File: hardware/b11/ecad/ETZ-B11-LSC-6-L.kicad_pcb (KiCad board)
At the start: 2 copper layers, 112.3 x 85.8 mm, 0 parts

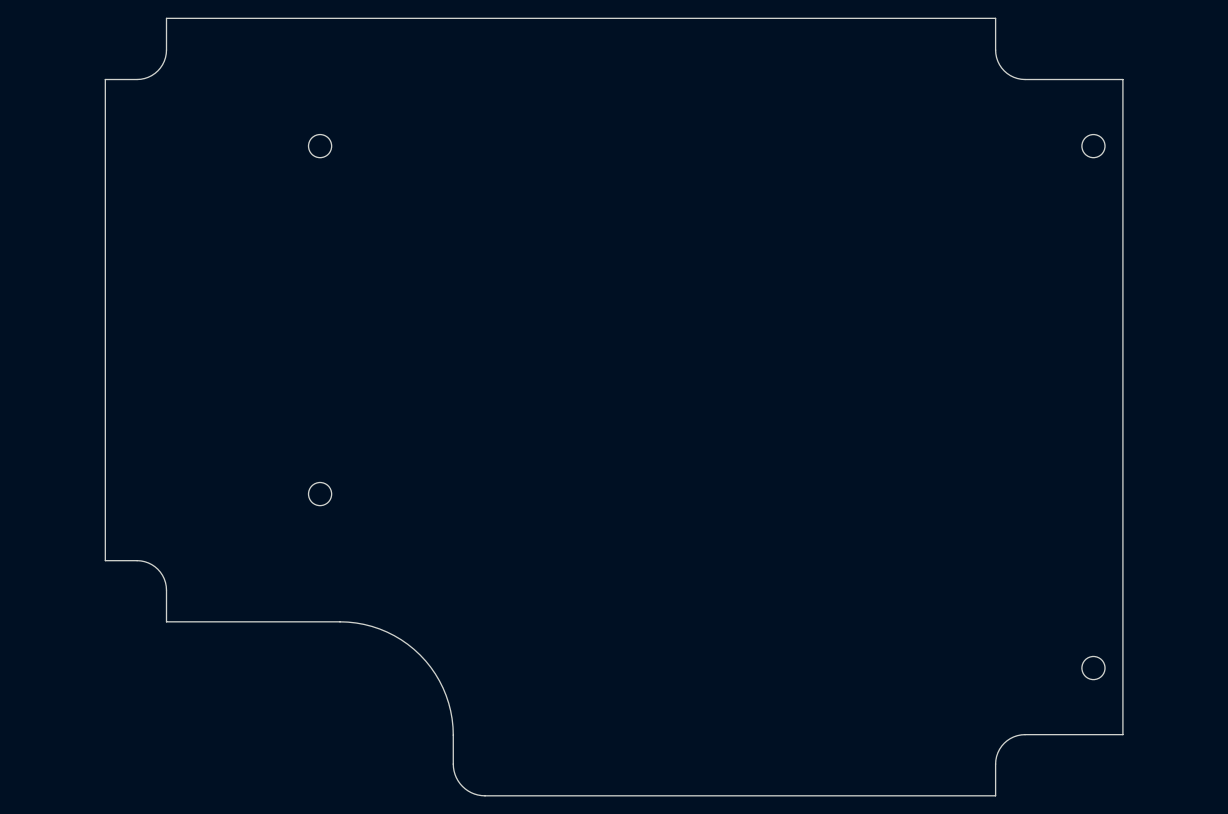
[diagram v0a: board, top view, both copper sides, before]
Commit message: fix(hardware/b11): correct 6-col PCB outlines and regenerate all boards
Update DXF outlines for all 6-col variants (LSC, RSC, LSP, RSP — both
normal and low profile) exported manually from OnShape with the _6
configuration. Regenerate all 16 KiCad PCBs from the corrected outlines
and re-place MX hotswap switches on the 4 normal-profile carrier boards.

Co-Authored-By: Claude Sonnet 4.6 <noreply@anthropic.com>
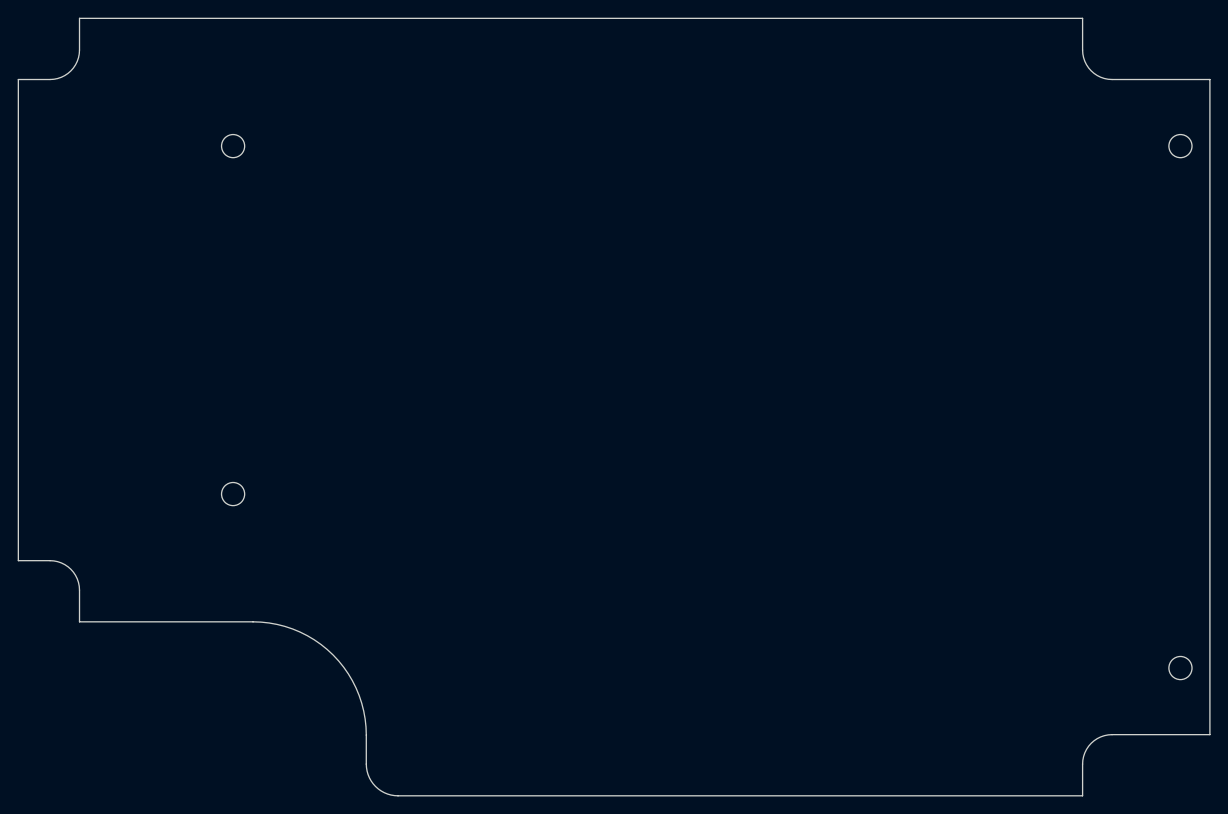
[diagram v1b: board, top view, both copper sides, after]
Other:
- board size 112.3 x 85.8 mm -> 131.5 x 85.8 mm
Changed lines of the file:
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@@
 		(allow_soldermask_bridges_in_footprints no)
 		(tenting front back)
-		(grid_origin 106.449999 73.3)
+		(grid_origin 96.85 73.3)
 		(pcbplotparams
 			(layerselection 0x00000000_00000000_55555555_5755f5ff)
@@
 	(net 0 "")
 	(gr_line
-		(start 95.85 65.95)
-		(end 92.35 65.95)
-		(stroke
-			(width 0.05)
-			(type default)
-		)
-		(layer "Edge.Cuts")
-	)
-	(gr_arc
-		(start 190.6 141.5)
-		(mid 191.551903 139.201903)
-		(end 193.85 138.25)
-		(stroke
-			(width 0.05)
-			(type default)
-		)
-		(layer "Edge.Cuts")
-	)
-	(gr_line
-		(start 193.85 138.25)
-		(end 204.65 138.25)
-		(stroke
-			(width 0.05)
-			(type default)
-		)
-		(layer "Edge.Cuts")
-	)
-	(gr_line
-		(start 190.6 141.5)
-		(end 190.6 145)
-		(stroke
-			(width 0.05)
-			(type default)
-		)
-		(layer "Edge.Cuts")
-	)
-	(gr_circle
-		(center 201.399999 130.9)
-		(end 202.675 130.9)
-		(stroke
-			(width 0.05)
-			(type default)
-		)
-		(fill no)
-		(layer "Edge.Cuts")
-	)
-	(gr_line
-		(start 95.85 119.05)
-		(end 92.35 119.05)
-		(stroke
-			(width 0.05)
-			(type default)
-		)
-		(layer "Edge.Cuts")
-	)
-	(gr_line
-		(start 92.35 65.95)
-		(end 92.35 119.05)
-		(stroke
-			(width 0.05)
-			(type default)
-		)
-		(layer "Edge.Cuts")
-	)
-	(gr_line
-		(start 193.85 65.95)
-		(end 204.65 65.95)
-		(stroke
-			(width 0.05)
-			(type default)
-		)
-		(layer "Edge.Cuts")
-	)
-	(gr_line
-		(start 134.25 145)
-		(end 190.6 145)
-		(stroke
-			(width 0.05)
-			(type default)
-		)
-		(layer "Edge.Cuts")
-	)
-	(gr_line
-		(start 99.1 62.7)
-		(end 99.1 59.2)
-		(stroke
-			(width 0.05)
-			(type default)
-		)
-		(layer "Edge.Cuts")
-	)
-	(gr_line
-		(start 204.65 138.25)
-		(end 204.649999 65.95)
-		(stroke
-			(width 0.05)
-			(type default)
-		)
-		(layer "Edge.Cuts")
-	)
-	(gr_arc
-		(start 95.85 119.05)
-		(mid 98.148097 120.001903)
-		(end 99.1 122.3)
-		(stroke
-			(width 0.05)
-			(type default)
-		)
-		(layer "Edge.Cuts")
-	)
-	(gr_line
-		(start 190.6 59.2)
-		(end 99.1 59.2)
-		(stroke
-			(width 0.05)
-			(type default)
-		)
-		(layer "Edge.Cuts")
-	)
-	(gr_circle
-		(center 116.05 73.3)
-		(end 117.324999 73.3)
-		(stroke
-			(width 0.05)
-			(type default)
-		)
-		(fill no)
-		(layer "Edge.Cuts")
-	)
-	(gr_circle
-		(center 201.399999 73.3)
-		(end 202.675 73.3)
-		(stroke
-			(width 0.05)
-			(type default)
-		)
-		(fill no)
-		(layer "Edge.Cuts")
-	)
-	(gr_line
-		(start 99.1 122.3)
-		(end 99.1 125.8)
-		(stroke
-			(width 0.05)
-			(type default)
-		)
-		(layer "Edge.Cuts")
-	)
-	(gr_circle
-		(center 116.05 111.7)
-		(end 117.324999 111.7)
-		(stroke
-			(width 0.05)
-			(type default)
-		)
-		(fill no)
-		(layer "Edge.Cuts")
-	)
-	(gr_arc
-		(start 99.1 62.7)
-		(mid 98.148097 64.998097)
-		(end 95.85 65.95)
-		(stroke
-			(width 0.05)
-			(type default)
-		)
-		(layer "Edge.Cuts")
-	)
-	(gr_line
-		(start 190.6 62.7)
-		(end 190.6 59.2)
-		(stroke
-			(width 0.05)
-			(type default)
-		)
-		(layer "Edge.Cuts")
-	)
-	(gr_arc
-		(start 118.25 125.8)
-		(mid 127.088835 129.461165)
-		(end 130.75 138.3)
-		(stroke
-			(width 0.05)
-			(type default)
-		)
-		(layer "Edge.Cuts")
-	)
-	(gr_arc
-		(start 193.85 65.95)
-		(mid 191.551903 64.998097)
-		(end 190.6 62.7)
-		(stroke
-			(width 0.05)
-			(type default)
-		)
-		(layer "Edge.Cuts")
-	)
-	(gr_line
-		(start 130.75 138.3)
-		(end 130.75 141.5)
-		(stroke
-			(width 0.05)
-			(type default)
-		)
-		(layer "Edge.Cuts")
-	)
-	(gr_line
-		(start 99.1 125.8)
-		(end 118.25 125.8)
-		(stroke
-			(width 0.05)
-			(type default)
-		)
-		(layer "Edge.Cuts")
-	)
-	(gr_arc
-		(start 134.25 145)
-		(mid 131.775126 143.974874)
-		(end 130.75 141.5)
-		(stroke
-			(width 0.05)
+		(start 121.15 138.3)
+		(end 121.15 141.5)
+		(stroke
+			(width 0.05)
+			(type default)
+		)
+		(layer "Edge.Cuts")
+	)
+	(gr_line
+		(start 89.5 122.3)
+		(end 89.5 125.799999)
+		(stroke
+			(width 0.05)
+			(type default)
+		)
+		(layer "Edge.Cuts")
+	)
+	(gr_line
+		(start 214.25 138.25)
+		(end 214.25 65.95)
+		(stroke
+			(width 0.05)
+			(type default)
+		)
+		(layer "Edge.Cuts")
+	)
+	(gr_circle
+		(center 211 73.3)
+		(end 212.275 73.3)
+		(stroke
+			(width 0.05)
+			(type default)
+		)
+		(fill no)
+		(layer "Edge.Cuts")
+	)
+	(gr_line
+		(start 124.65 145)
+		(end 200.2 145)
+		(stroke
+			(width 0.05)
+			(type default)
+		)
+		(layer "Edge.Cuts")
+	)
+	(gr_circle
+		(center 211 130.9)
+		(end 212.275 130.9)
+		(stroke
+			(width 0.05)
+			(type default)
+		)
+		(fill no)
+		(layer "Edge.Cuts")
+	)
+	(gr_line
+		(start 203.45 65.95)
+		(end 214.25 65.95)
+		(stroke
+			(width 0.05)
+			(type default)
+		)
+		(layer "Edge.Cuts")
+	)
+	(gr_arc
+		(start 89.5 62.7)
+		(mid 88.548097 64.998097)
+		(end 86.25 65.95)
+		(stroke
+			(width 0.05)
+			(type default)
+		)
+		(layer "Edge.Cuts")
+	)
+	(gr_line
+		(start 89.5 125.799999)
+		(end 108.65 125.799999)
+		(stroke
+			(width 0.05)
+			(type default)
+		)
+		(layer "Edge.Cuts")
+	)
+	(gr_arc
+		(start 108.65 125.8)
+		(mid 117.488835 129.461165)
+		(end 121.15 138.3)
+		(stroke
+			(width 0.05)
+			(type default)
+		)
+		(layer "Edge.Cuts")
+	)
+	(gr_arc
+		(start 124.65 145)
+		(mid 122.175126 143.974874)
+		(end 121.15 141.5)
+		(stroke
+			(width 0.05)
+			(type default)
+		)
+		(layer "Edge.Cuts")
+	)
+	(gr_line
+		(start 200.2 59.199999)
+		(end 89.5 59.2)
+		(stroke
+			(width 0.05)
+			(type default)
+		)
+		(layer "Edge.Cuts")
+	)
+	(gr_arc
+		(start 86.25 119.05)
+		(mid 88.548097 120.001903)
+		(end 89.5 122.3)
+		(stroke
+			(width 0.05)
+			(type default)
+		)
+		(layer "Edge.Cuts")
+	)
+	(gr_arc
+		(start 200.2 141.5)
+		(mid 201.151903 139.201903)
+		(end 203.45 138.25)
+		(stroke
+			(width 0.05)
+			(type default)
+		)
+		(layer "Edge.Cuts")
+	)
+	(gr_circle
+		(center 106.45 73.3)
+		(end 107.725 73.3)
+		(stroke
+			(width 0.05)
+			(type default)
+		)
+		(fill no)
+		(layer "Edge.Cuts")
+	)
+	(gr_circle
+		(center 106.45 111.7)
+		(end 107.725 111.7)
+		(stroke
+			(width 0.05)
+			(type default)
+		)
+		(fill no)
+		(layer "Edge.Cuts")
+	)
+	(gr_arc
+		(start 203.45 65.95)
+		(mid 201.151903 64.998097)
+		(end 200.2 62.7)
+		(stroke
+			(width 0.05)
+			(type default)
+		)
+		(layer "Edge.Cuts")
+	)
+	(gr_line
+		(start 200.2 141.5)
+		(end 200.2 145)
+		(stroke
+			(width 0.05)
+			(type default)
+		)
+		(layer "Edge.Cuts")
+	)
+	(gr_line
+		(start 86.25 65.95)
+		(end 82.75 65.95)
+		(stroke
+			(width 0.05)
+			(type default)
+		)
+		(layer "Edge.Cuts")
+	)
+	(gr_line
+		(start 86.25 119.05)
+		(end 82.75 119.05)
+		(stroke
+			(width 0.05)
+			(type default)
+		)
+		(layer "Edge.Cuts")
+	)
+	(gr_line
+		(start 200.2 62.7)
+		(end 200.2 59.199999)
+		(stroke
+			(width 0.05)
+			(type default)
+		)
+		(layer "Edge.Cuts")
+	)
+	(gr_line
+		(start 203.45 138.25)
+		(end 214.25 138.25)
+		(stroke
+			(width 0.05)
+			(type default)
+		)
+		(layer "Edge.Cuts")
+	)
+	(gr_line
+		(start 89.5 62.7)
+		(end 89.5 59.2)
+		(stroke
+			(width 0.05)
+			(type default)
+		)
+		(layer "Edge.Cuts")
+	)
+	(gr_line
+		(start 82.75 65.95)
+		(end 82.75 119.05)
+		(stroke
+			(width 0.05)

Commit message: feat(hardware/b11): place hotswap sockets on all carrier boards, south-facing
- Place Kailh MX hotswap sockets (MX-Hotswap-1U) on 4 normal-profile carrier
  boards at 19.2mm pitch, flipped to B.Cu, 180° south-facing orientation
- Place Kailh Choc v1 hotswap sockets (PG1350) on 4 low-profile carrier boards
  at 19.2mm pitch, 180° south-facing orientation
- Add 3D model (Kailh-Choc-Socket-CPG135001S30.step) to PG1350 footprint with
  correct offset/rotation for B.Cu-pad, F.Cu-module placement
- Strip F.SilkS, F.Fab, F.CrtYd top-layer graphics from LP carrier PG1350 footprints
- Rename place-b11-switches.py → place-b11-switches-np.py for symmetry with new lp script
- Add place-b11-switches-lp.py for Choc v1 placement automation

Co-Authored-By: Claude Sonnet 4.6 <noreply@anthropic.com>
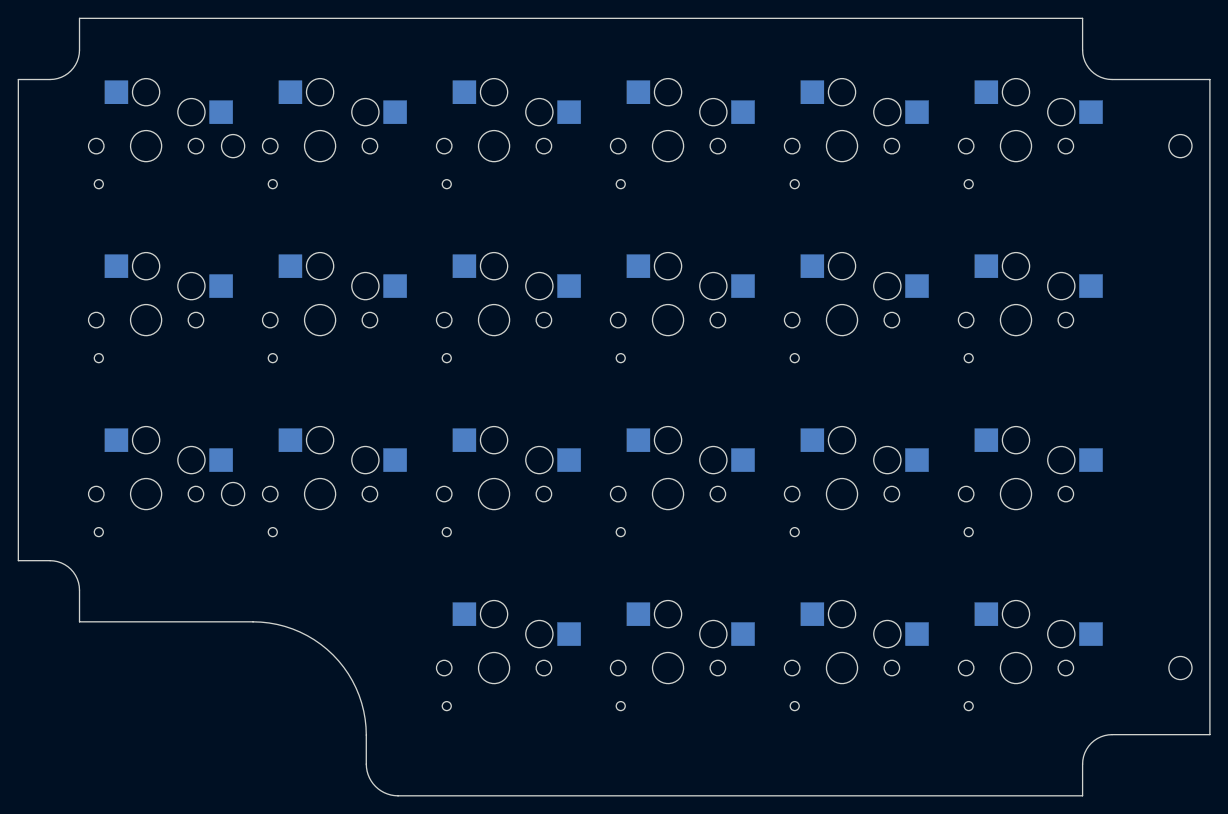
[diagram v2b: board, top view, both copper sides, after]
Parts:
- added SW1: Kailh_socket_PG1350, Kailh_socket_PG1350, F.Cu at (96.8, 73.3)
- added SW10: Kailh_socket_PG1350, Kailh_socket_PG1350, F.Cu at (154.4, 92.5)
- added SW11: Kailh_socket_PG1350, Kailh_socket_PG1350, F.Cu at (173.6, 92.5)
- added SW12: Kailh_socket_PG1350, Kailh_socket_PG1350, F.Cu at (192.8, 92.5)
- added SW13: Kailh_socket_PG1350, Kailh_socket_PG1350, F.Cu at (96.8, 111.7)
- added SW14: Kailh_socket_PG1350, Kailh_socket_PG1350, F.Cu at (116.0, 111.7)
- added SW15: Kailh_socket_PG1350, Kailh_socket_PG1350, F.Cu at (135.2, 111.7)
- added SW16: Kailh_socket_PG1350, Kailh_socket_PG1350, F.Cu at (154.4, 111.7)
- added SW17: Kailh_socket_PG1350, Kailh_socket_PG1350, F.Cu at (173.6, 111.7)
- added SW18: Kailh_socket_PG1350, Kailh_socket_PG1350, F.Cu at (192.8, 111.7)
- added SW19: Kailh_socket_PG1350, Kailh_socket_PG1350, F.Cu at (135.2, 130.9)
- added SW2: Kailh_socket_PG1350, Kailh_socket_PG1350, F.Cu at (116.0, 73.3)
- added SW20: Kailh_socket_PG1350, Kailh_socket_PG1350, F.Cu at (154.4, 130.9)
- added SW21: Kailh_socket_PG1350, Kailh_socket_PG1350, F.Cu at (173.6, 130.9)
- added SW22: Kailh_socket_PG1350, Kailh_socket_PG1350, F.Cu at (192.8, 130.9)
- added SW3: Kailh_socket_PG1350, Kailh_socket_PG1350, F.Cu at (135.2, 73.3)
- added SW4: Kailh_socket_PG1350, Kailh_socket_PG1350, F.Cu at (154.4, 73.3)
- added SW5: Kailh_socket_PG1350, Kailh_socket_PG1350, F.Cu at (173.6, 73.3)
- added SW6: Kailh_socket_PG1350, Kailh_socket_PG1350, F.Cu at (192.8, 73.3)
- added SW7: Kailh_socket_PG1350, Kailh_socket_PG1350, F.Cu at (96.8, 92.5)
- added SW8: Kailh_socket_PG1350, Kailh_socket_PG1350, F.Cu at (116.0, 92.5)
- added SW9: Kailh_socket_PG1350, Kailh_socket_PG1350, F.Cu at (135.2, 92.5)

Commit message: feat(hardware/b11): add SMD 6028 back-mount LED footprint and place on all carrier PCBs
- Add LED_SMD_6028_BackMount footprint with router-safe rounded-rectangle
  slot cutout (3.3 × 3.9 mm, 0.5 mm corners, 1 mm bit), roundrect pads
  (1.4 × 2.8 mm, 25% ratio), silkscreen polarity markers clear of pads
- Add LED_SMD_6028.step 3D model from 3D Content Central
- Add place-b11-leds.py: places 18–22 LEDs per carrier PCB aligned to
  the switch grid, 5.9 mm south of each switch center
- Place LEDs on all 8 carrier PCBs (LSC/RSC × 5/6-col × N/L)

Co-Authored-By: Claude Sonnet 4.6 <noreply@anthropic.com>
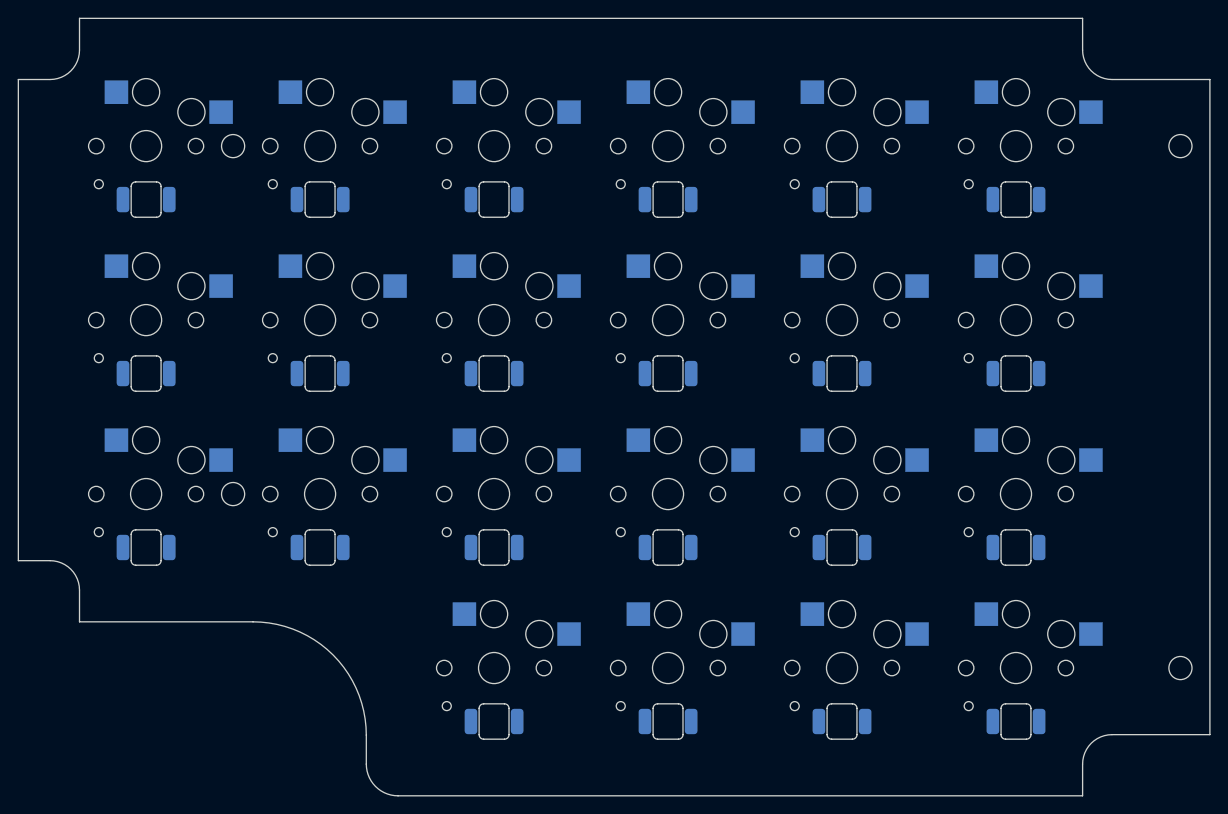
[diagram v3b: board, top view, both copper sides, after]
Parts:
- added LED1: LED_SMD_6028_BackMount, LED_SMD_6028_BackMount, B.Cu at (96.8, 79.2)
- added LED10: LED_SMD_6028_BackMount, LED_SMD_6028_BackMount, B.Cu at (154.4, 98.4)
- added LED11: LED_SMD_6028_BackMount, LED_SMD_6028_BackMount, B.Cu at (173.6, 98.4)
- added LED12: LED_SMD_6028_BackMount, LED_SMD_6028_BackMount, B.Cu at (192.8, 98.4)
- added LED13: LED_SMD_6028_BackMount, LED_SMD_6028_BackMount, B.Cu at (96.8, 117.6)
- added LED14: LED_SMD_6028_BackMount, LED_SMD_6028_BackMount, B.Cu at (116.0, 117.6)
- added LED15: LED_SMD_6028_BackMount, LED_SMD_6028_BackMount, B.Cu at (135.2, 117.6)
- added LED16: LED_SMD_6028_BackMount, LED_SMD_6028_BackMount, B.Cu at (154.4, 117.6)
- added LED17: LED_SMD_6028_BackMount, LED_SMD_6028_BackMount, B.Cu at (173.6, 117.6)
- added LED18: LED_SMD_6028_BackMount, LED_SMD_6028_BackMount, B.Cu at (192.8, 117.6)
- added LED19: LED_SMD_6028_BackMount, LED_SMD_6028_BackMount, B.Cu at (135.2, 136.8)
- added LED2: LED_SMD_6028_BackMount, LED_SMD_6028_BackMount, B.Cu at (116.0, 79.2)
- added LED20: LED_SMD_6028_BackMount, LED_SMD_6028_BackMount, B.Cu at (154.4, 136.8)
- added LED21: LED_SMD_6028_BackMount, LED_SMD_6028_BackMount, B.Cu at (173.6, 136.8)
- added LED22: LED_SMD_6028_BackMount, LED_SMD_6028_BackMount, B.Cu at (192.8, 136.8)
- added LED3: LED_SMD_6028_BackMount, LED_SMD_6028_BackMount, B.Cu at (135.2, 79.2)
- added LED4: LED_SMD_6028_BackMount, LED_SMD_6028_BackMount, B.Cu at (154.4, 79.2)
- added LED5: LED_SMD_6028_BackMount, LED_SMD_6028_BackMount, B.Cu at (173.6, 79.2)
- added LED6: LED_SMD_6028_BackMount, LED_SMD_6028_BackMount, B.Cu at (192.8, 79.2)
- added LED7: LED_SMD_6028_BackMount, LED_SMD_6028_BackMount, B.Cu at (96.8, 98.4)
- added LED8: LED_SMD_6028_BackMount, LED_SMD_6028_BackMount, B.Cu at (116.0, 98.4)
- added LED9: LED_SMD_6028_BackMount, LED_SMD_6028_BackMount, B.Cu at (135.2, 98.4)
